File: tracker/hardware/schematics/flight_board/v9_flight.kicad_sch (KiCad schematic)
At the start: 18 parts, among them U1 ESP32-S3-WROOM-1U-N8R8, U2 LoRa2021F33-2G4, U3 LoRa2021_Castellated, U4 SX1280, U5 MAX-M10S, U6 MS5611-01BA, U7 TPS7A02

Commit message: sch(v9): provision the F33 PA rail for the module maximum draw (ADR-044a)
v9 target only; the C3 target's output is unchanged.

Implements ADR-044a / ADR-044 option (a):
* U2 pin 1 = F33_VCC, fed PRE-LDO from VSCAP through the ADR-029 D8 pin-1
  selector J_VCC (pin2 common; pin1 VSCAP for the F33; pin3 +3V3 for the bare
  LoRa2021). Never through the TPS7A02 (<=300 mA vs 1118 mA).
* C_BULK 100uF + C_HF 100nF at the module pin (docs/PCB-HANDOVER-FOR-JLCPCB 2.4)
* D_CLAMP TVS across F33_VCC (set point TODO(unverified), OPEN-16)
* R_MON1/R_MON2 4.7M + C_MON -> F33_VSENSE -> ESP32-S3 IO13 (U1 pin 21)
* supercap bank wired as a real SERIES pair (new SCAP_MID) + the 2x 10k
  balancing resistors ADR-006/ADR-044 mandate but the sheet omitted
* GNSS moved onto its own filtered rail (GNSS_VCC) per ADR-029 2(d); the sheet
  had R_F1 pin 1 in two nets and R_F1 pin 2 floating

ERC closer set (each cited): U2.1, U5.6/7/9, U7.3, U1.21, C_CAP1.2, R_F1.2,
plus the slave-MISO pin-type correction that removes the false pin_to_pin.
Open pins keep explicit TODO(unverified) markers; nothing is tied off by
guessing and no ERC error is suppressed. V9_TODO is now 19 open questions.

Also hardens the generator: a (ref,pin) may be in exactly one net (the R_F1
defect above was invisible without it), and PWR_FLAG stubs are placed
collision-aware (a fixed +5.08 offset had merged GNSS_VCC into +3V3).
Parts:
- removed U6: MS5611-01BA, Package_LGA:LGA-8_3x5mm_P1.25mm, symbol Sensor_Pressure:MS5611-01BA
- added C_BULK: 100uF, Capacitor_SMD:C_1206_3216Metric, symbol Device:C
- added C_HF: 100nF, Capacitor_SMD:C_0402_1005Metric, symbol Device:C
- added C_MON: 10nF, Capacitor_SMD:C_0402_1005Metric, symbol Device:C
- added D_CLAMP: TVS clamp (set point TODO(unverified)), Diode_SMD:D_SOD-323, symbol Device:D_TVS
- added J_VCC: F33_VCC_SEL, Jumper:SolderJumper-3_P1.3mm_Open_RoundedPad1.0x1.5mm, symbol Jumper:SolderJumper_3_Open
- added R_BAL1, R_BAL2: 10k, Resistor_SMD:R_0402_1005Metric, symbol Device:R
- added R_MON1, R_MON2: 4.7M, Resistor_SMD:R_0402_1005Metric, symbol Device:R
- added U7: TPS7A02, Package_TO_SOT_SMD:SOT-23-5, symbol balloon_flight_v9:TPS7A0233
- U6: renamed from U7; value TPS7A02 -> MS5611-01BA; footprint Package_TO_SOT_SMD:SOT-23-5 -> Package_LGA:LGA-8_3x5mm_P1.25mm; symbol balloon_flight_v9:TPS7A0233 -> Sensor_Pressure:MS5611-01BA
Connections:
- net +3V3: now also R_F1.1, U5.6 (V_BCKP), U5.7 (VCC_IO), U5.9 (~{RESET}), U6.1 (VDD), J_VCC.3 (B), U7.5 (OUT); no longer U5.8 (VCC), U6.5 (OUT)
- net GND: now also U6.3 (GND), C_BULK.2, C_HF.2, C_MON.2, D_CLAMP.2 (A2), R_BAL2.2, R_MON2.2, U7.2 (GND); no longer U6.2 (GND)
- net I2C_SCL: now also U6.8 (SCLK)
- net I2C_SDA: now also U6.7 (SDI/SDA)
- net VSCAP: now also J_VCC.1 (A), R_BAL1.1, U7.1 (IN), U7.3 (EN); no longer C4.1, C_CAP2.1, R_F1.1, U6.1 (IN)
- net F33_VCC: now reaches U2.1 (VCC)
- net F33_VCC: now also C_BULK.1, C_HF.1, D_CLAMP.1 (A1), J_VCC.2 (C), R_MON1.1
- net SCAP_MID: now reaches C_CAP1.2
- net SCAP_MID: now also C_CAP2.1, R_BAL1.2, R_BAL2.1
- net F33_VSENSE: now reaches U1.21 (IO13)
- net F33_VSENSE: now also C_MON.1, R_MON1.2, R_MON2.1
- net at U6.4 (CSB): now also U6.5 (CSB)
- net GNSS_VCC: now reaches R_F1.2
- net GNSS_VCC: now also C4.1, U5.8 (VCC)
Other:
- note added: "ADR-044a (operator directive 2026-10-07): F33 pin 1 VCC is provisioned for the MODULE MAXIMUM DRAW (1118 mA @ 5.5 V = 6.15 W DC) and is fed from the RAW supercap node (VSCAP, post-BAT54, PRE-LDO) through the ADR-029 D8 pin-1 selector J_VCC. It is NEVER fed through the TPS7A02 (<=300 mA vs 1118 mA = hard failure). Local bulk C_BULK + C_HF, clamp D_CLAMP, rail monitor R_MON1/R_MON2/C_MON -> IO13. F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"
- note added: "BALLOON v9 TRI-BAND FLIGHT BOARD - DESIGN-INTENT schematic from the v9 decision records (ADR-029/034/035/036-043, ADR-044/044a/045). NOT derived from a PCB."
- note added: "F33 RAIL PROVISION (ADR-044a): pin-1 selector / bulk / clamp / monitor"
- note added: "SUPERCAP BANK (SERIES + BALANCING) / BAT54 / DIVIDER / GNSS RC"
- note added: "TODO(unverified) OPEN-1 SX1280 SUPPLY (U4 pins 1,2) -- SX1280 VDD_IN/VDD_IO rail not fixed by any record and the Semtech datasheet is unreachable here. Left open deliberately."
- note added: "TODO(unverified) OPEN-10 ESP32-S3 EN and USB (U1 pins 3,13,14) -- Module EN strap and the USB_D-/USB_D+ pads have no v9 connector or recorded tie-off. The ADR-029 pin plan calls USB-Serial-JTAG the assumed debug path, so these are not unused - they lack a termination. The reset RC is also absent from the v9 BOM (docs/coordination/SCHEMATIC-PLAN-3VARIANTS.md 5 item 2)."
- note added: "TODO(unverified) OPEN-11 SUPERCAP ADC GPIO -- ADR-006 puts the supercap ADC on GPIO0; the ADR-029 pin plan reserves IO0 as a boot strap and forbids loading it. The divider tap net exists but its MCU end is unresolved. (Note: this sheet's NEW rail monitor does not use GPIO0 - see OPEN-17.)"
- note added: "TODO(unverified) OPEN-12 SOLAR INPUT SOURCE -- The 4-wing x 3-cell solar array input connector is not in the v9 component list; SOLAR_IN has only the D1 anode end so far."
- note added: "TODO(unverified) OPEN-13 SX1280 PIN NUMBERS + LAND PATTERN -- The Semtech SX1280 datasheet could not be retrieved on this host. The symbol's QFN pad numbering and SX1280_QFN24.kicad_mod geometry are PLACEHOLDERS - every SX1280 pin is TODO(unverified). ADR-045 D1 files the same gap as a blocker for its antenna-access gate."
- note added: "TODO(unverified) OPEN-14 UNASSIGNED ESP32-S3 GPIO (U1 pins 20,24,25 = IO12, IO47, IO48) -- The ADR-029 pin plan does not assign these, and the strapping audit only clears IO0/IO3/IO45/IO46 as straps and IO35-IO37 as PSRAM. Left floating rather than guessed: assign them deliberately in a pin-plan revision, or mark them no_connect on the record."
- note added: "TODO(unverified) OPEN-15 SUPERCAP CELL ESR + COLD BANK BEHAVIOUR -- ADR-044a 3/4: the AVX SCC 3.3 F 2.7 V cell's ESR is NOT in this repository, at 25 C or at -60 C. Every rail-step number in ADR-044a is conditional on the assumed 0.10 Ohm/cell. ADR-029 5 test 4 (<20 mV rail dip during a worst-case burst) is NOT met by scaling this cell family: 16.7 mOhm would need ~12 cells in parallel per series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"
- note added: "TODO(unverified) OPEN-16 CLAMP SET POINT (D_CLAMP) -- ADR-044a 7: the clamp must conduct above the 5.4 V rail top and below the F33's damage threshold, which Rev 1.1 of the datasheet does not publish; the 12-cell array's open-circuit voltage at -60 C is also unmeasured. Part and set point cannot be finalised - do not order a guess."
- note added: "TODO(unverified) OPEN-17 RAIL-MONITOR ADC CHANNEL (U1 pin 21 = IO13) -- ADR-044a 6: IO13 is unassigned by the ADR-029 pin plan, and ADR-038 D1 makes Wi-Fi/BT never enabled (CONFIG_ESP_WIFI_ENABLED=n), which is the condition normally attached to ESP32-S3 ADC2 use. Those two facts are the whole basis for putting the monitor there. The ADC channel number and the ADC's required source impedance are N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"
- note added: "TODO(unverified) OPEN-18 O5 EVIDENCE STILL OPEN -- ADR-029 O5 / ADR-044 7: no 5 V chain demonstrated at >=1.2 A load-step capability, no 3.3 V rail at >=0.60 A transient, no cold supercap or regulator evidence, no ADR-029 5 test 4. ADR-044a sizes for the maximum draw; it does not measure the chain. The BOM freeze stays gated on this."
- note added: "TODO(unverified) OPEN-19 ANTENNA SOLDER ACCESS (ADR-045) -- ADR-045 does NOT change the antenna connector count or these net names: ADR-029 D3's four U.FL feeds stand, and ADR-045 gates PLACEMENT, not netlist. Its requirement is that every antenna-port pad of BOTH LoRa2021 modules, of the SX1280 and of the GNSS feed be reachable by a soldering iron from OUTSIDE the module body, enforced by tracke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"
- note added: "TODO(unverified) OPEN-2 SX1280 RF PORT (U4 pin 14 RFIO) -- No antenna feed is assigned to the SX1280 RFIO. ADR-029 D3 enumerates the FOUR connectors as {GNSS, F33 sub-GHz, F33 ANT-2G4, SX1280}, but ADR-034 D1 re-points the 2.4 GHz RX at a SEPARATE bare LoRa2021 that also needs a feed. Exactly one of the two is left without a listed feed - resolve before fabricating. No tie-off guessed. ADR-045 D1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"
- note added: "TODO(unverified) OPEN-3 BARE-MODULE CONTROL LINES (U3 pins 6,7,14,15) -- ADR-034 adds the bare LoRa2021 but NO record assigns its NSS/BUSY/RESET/IRQ GPIOs (the ADR-029 pin plan predates ADR-034). Left floating - the +4 GPIO budget in V9-RADIO-SITE-MATRIX 3.1 must be spent first."
- note added: "TODO(unverified) OPEN-4 BARE-MODULE SUB-GHz PORT (U3 pin 9 ANT) -- Unused under ADR-034 (U3 is the 2.4 GHz RX). An RF port is not tied off without a decision - left open."
- note added: "TODO(unverified) OPEN-5 BARE-MODULE PAD FUNCTIONS (U3 pins 13,16,17) -- PAD13/PAD16/PAD17 functions are unverified (v8i audit: DECLARED_GAP)."
- note added: "TODO(unverified) OPEN-6 F33 DIO5 (U1 pin 19) -- The pin plan assigns F33_DIO5 to GPIO11, but the F33's 18-pad map has no DIO5 pad. Which F33 pad carries DIO5 is unresolved - left open."
- note added: "TODO(unverified) OPEN-7 MS5611 TIE-OFFS (U6 pins 2,4,6) -- MS5611 PS / CSB / SDO tie-off levels (I2C mode) are not in any record. The v8i board's barometer pads are NOT transferable: v8i fits a Bosch LGA-8 2.5x2.5 mm footprint, this design fits LGA-8 3x5 mm."
- note added: "TODO(unverified) OPEN-8 MAX-M10S TIE-OFFS (U5 pins 15,18) -- VIO_SEL (15) and ~SAFEBOOT (18) were netless DECLARED_GAP pins on the frozen v8i board and no record fixes them. V_BCKP / VCC_IO / ~RESET (pins 6/7/9) are NO LONGER open: the v8i board - same ublox_MAX footprint and same RF_GPS:MAX-M10S symbol - ties 6/7/8/9 to +3V3, and this sheet follows that precedent."
- note added: "TODO(unverified) OPEN-9 TPS7A02 NC (U7 pin 4) -- TPS7A02 pin 4 is a real pad with an unverified function: the v8i board leaves it netless (DECLARED_GAP 'TPS7A02 pin 4 function / tie-off'), and no datasheet for the part is committed here. Deliberately NOT given an invented tie-off or a no_connect flag, because the flag would assert a decision no record makes."
- note added: "U2 LoRa2021F33-2G4 (433 MHz TX) - VCC PRE-LDO, ADR-044a"
- note removed: "BALLOON v9 TRI-BAND FLIGHT BOARD - DESIGN-INTENT schematic from the v9 decision records (ADR-029/034/035/036-043). NOT derived from a PCB."
- note removed: "SUPERCAP BANK / BAT54 / DIVIDER / GNSS RC"
- note removed: "TODO(unverified) OPEN-1 5 V RAIL (U2 pin 1 VCC) -- The F33 reaches 2 W/33 dBm @433 only at 5.0 V. The 5 V rail is an open operator item (ADR-029 O5, carried into ADR-034). U2 pin 1 is left with NO net - do not tie a 2 W PA module to 3V3 or to an invented 5 V rail."
- note removed: "TODO(unverified) OPEN-10 TPS7A02 EN / NC (U7 pins 3,4) -- TPS7A02 EN strap and the pin-4 NC treatment are not in any record."
- note removed: "TODO(unverified) OPEN-11 ESP32-S3 EN and USB (U1 pins 3,13,14) -- Module EN strap and the USB_D-/USB_D+ pads have no v9 connector or recorded tie-off."
- note removed: "TODO(unverified) OPEN-12 SUPERCAP ADC GPIO -- ADR-006 puts the supercap ADC on GPIO0; the ADR-029 pin plan reserves IO0 as a boot strap. The divider tap net exists but its MCU end is unresolved."
- note removed: "TODO(unverified) OPEN-13 SOLAR INPUT SOURCE -- The 4-wing x 3-cell solar array input connector is not in the v9 component list; SOLAR_IN has only the D1 anode end so far."
- note removed: "TODO(unverified) OPEN-14 SX1280 PIN NUMBERS + LAND PATTERN -- The Semtech SX1280 datasheet could not be retrieved on this host. The symbol's QFN pad numbering and SX1280_QFN24.kicad_mod geometry are PLACEHOLDERS - every SX1280 pin is TODO(unverified)."
- note removed: "TODO(unverified) OPEN-2 SX1280 SUPPLY (U4 pins 1,2) -- SX1280 VDD_IN/VDD_IO rail not fixed by any record and the Semtech datasheet is unreachable here. Left open deliberately."
- note removed: "TODO(unverified) OPEN-3 SX1280 RF PORT (U4 pin 14 RFIO) -- No antenna feed is assigned to the SX1280 RFIO. ADR-029 D3 (as amended) enumerates the FOUR connectors as {GNSS, F33 sub-GHz, F33 ANT-2G4, SX1280}, but ADR-034 D1 re-points the 2.4 GHz RX at a SEPARATE bare LoRa2021 that also needs a feed. Exactly one of the two is left without a listed feed - resolve before fabricating. No tie-off guesse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"
- note removed: "TODO(unverified) OPEN-4 BARE-MODULE CONTROL LINES (U3 pins 6,7,14,15) -- ADR-034 adds the bare LoRa2021 but NO record assigns its NSS/BUSY/RESET/IRQ GPIOs (the ADR-029 pin plan predates ADR-034). Left floating - the +4 GPIO budget in V9-RADIO-SITE-MATRIX 3.1 must be spent first."
- note removed: "TODO(unverified) OPEN-5 BARE-MODULE SUB-GHz PORT (U3 pin 9 ANT) -- Unused under ADR-034 (U3 is the 2.4 GHz RX). An RF port is not tied off without a decision - left open."
- note removed: "TODO(unverified) OPEN-6 BARE-MODULE PAD FUNCTIONS (U3 pins 13,16,17) -- PAD13/PAD16/PAD17 functions are unverified (v8i audit: DECLARED_GAP)."
- note removed: "TODO(unverified) OPEN-7 F33 DIO5 (U1 pin 19) -- The pin plan assigns F33_DIO5 to GPIO11, but the F33's 18-pad map has no DIO5 pad. Which F33 pad carries DIO5 is unresolved - left open."
- note removed: "TODO(unverified) OPEN-8 MS5611 TIE-OFFS (U6 pins 2,4,6) -- MS5611 PS / CSB / SDO tie-off levels (I2C mode) are not in any record."
- note removed: "TODO(unverified) OPEN-9 MAX-M10S TIE-OFFS (U5 pins 6,7,9,15,18) -- V_BCKP / VCC_IO / ~RESET / VIO_SEL / ~SAFEBOOT tie-offs are not fixed by a record (VIO_SEL and ~SAFEBOOT were already DECLARED_GAP on v8i)."
- note removed: "U2 LoRa2021F33-2G4 (433 MHz TX, 5 V - RAIL OPEN)"

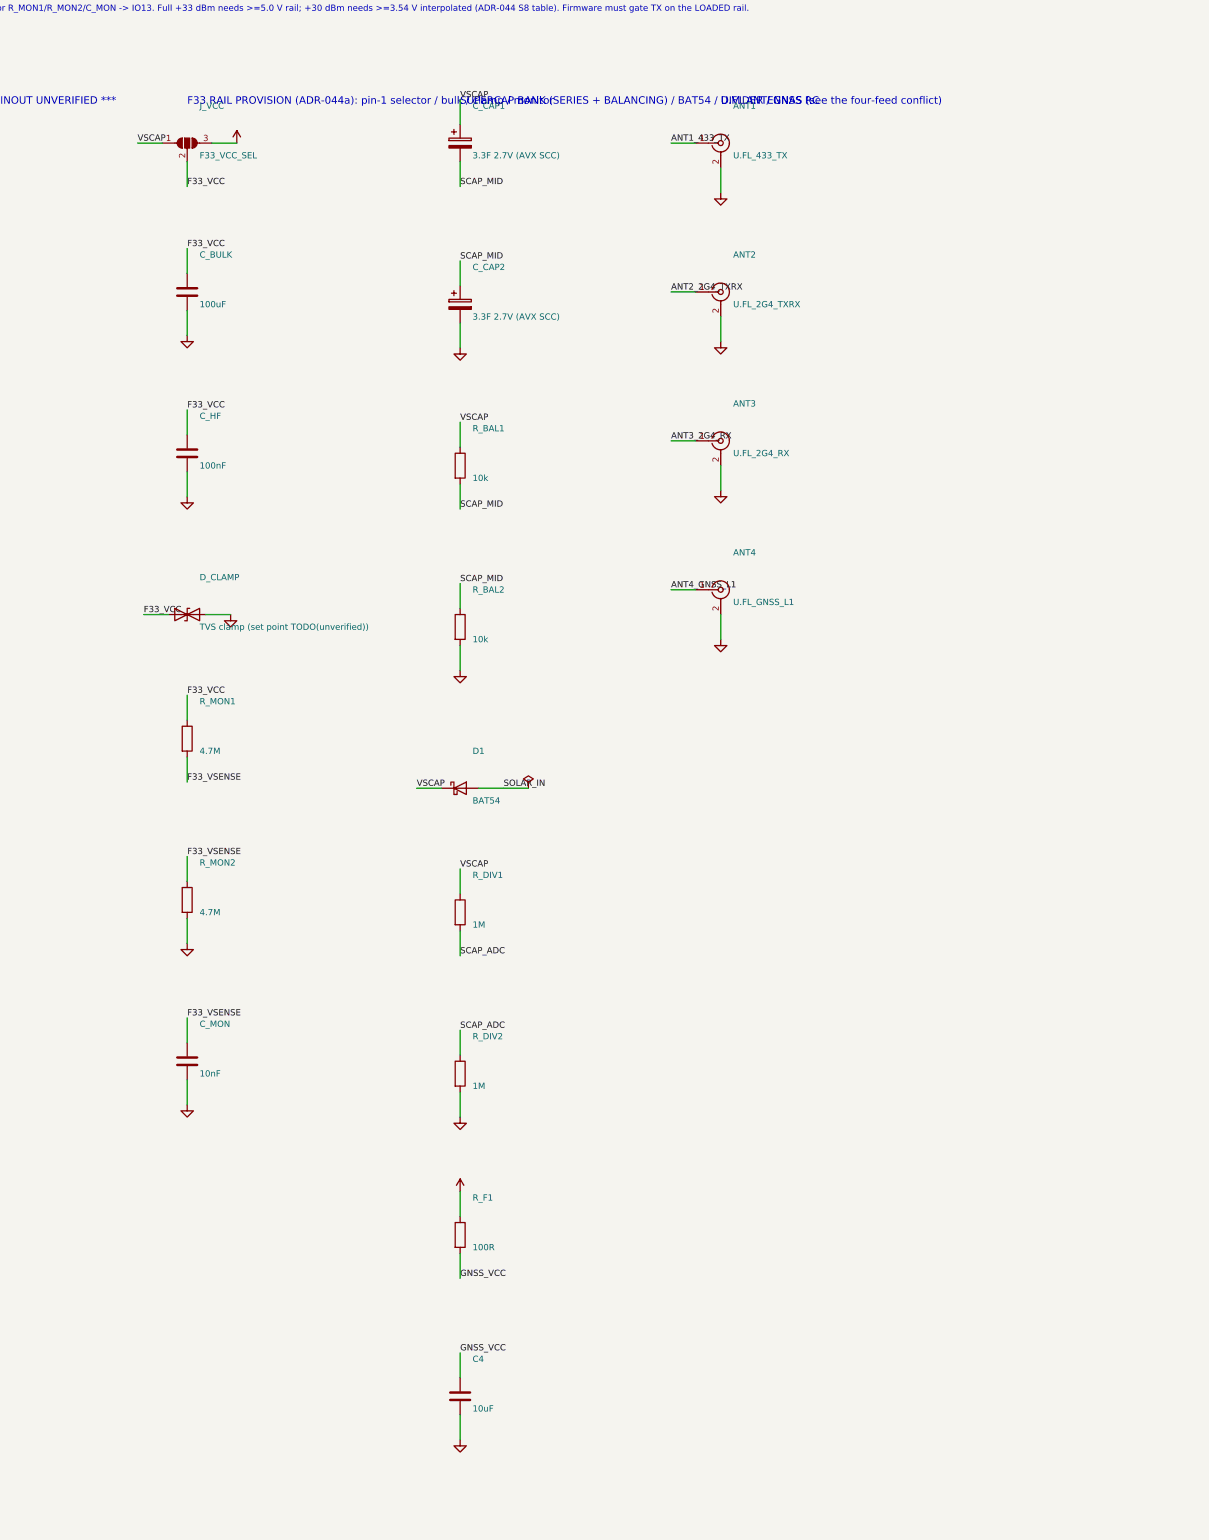
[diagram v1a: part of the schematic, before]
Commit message: sch(v9): final gate run + ADR-044a selector note (ERC 33 -> 24)
* J_VCC is drawn with a repo-local balloon_flight_v9 symbol instead of KiCad's
  Jumper library: the shared sym-lib-table is written by BOTH generators and the
  C3 union does not carry Jumper, so a stock-library symbol left the v9 sheet
  unresolvable after a C3 regeneration (observed: lib_symbol_issues warning).
  Now generation-order independent - verified 24 errors / 0 warnings both before
  and after the C3 target is regenerated.
* v9 gate: 24 ERC errors (24 pin_not_connected), 0 warnings, exit 5,
  deterministic sha256 dd8c6ed7...; 27 components, 35 nets.
* C3 gate: ALL GATES PASS, 0 errors / 1 warning (unchanged);
  v_c3_flight.kicad_sch byte-identical to base (4dd7e3fc...522c).
* v_c3_flight.net / v_c3_flight-erc.rpt restored to committed content (a re-run
  only rewrites the embedded absolute path + timestamp; net lists identical).

PROGRESS.md / REPORT.md stay untracked (.gitignore).
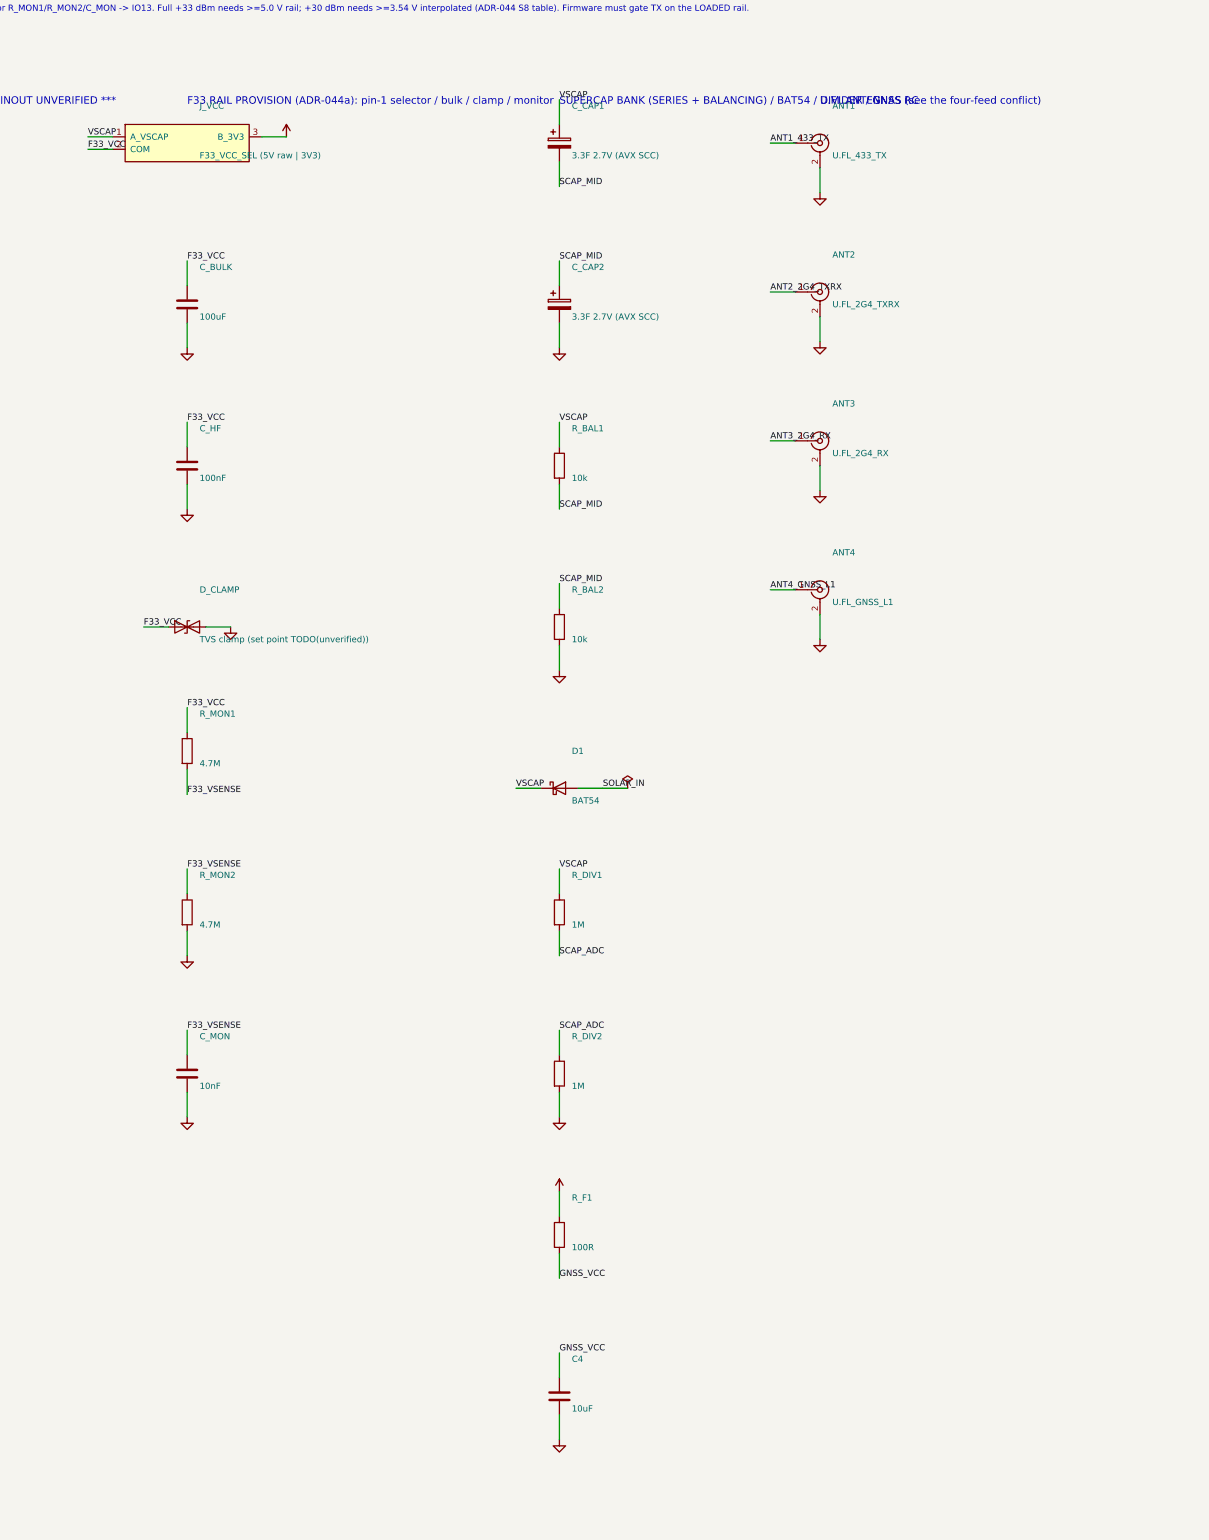
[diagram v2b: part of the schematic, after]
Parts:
- J_VCC: value F33_VCC_SEL -> F33_VCC_SEL (5V raw | 3V3); symbol Jumper:SolderJumper_3_Open -> balloon_flight_v9:F33_VCC_SEL
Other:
- moved on the sheet: ANT1, ANT2, ANT3, ANT4, C4, C_BULK, C_CAP1, C_CAP2, C_HF, C_MON, D1, D_CLAMP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
